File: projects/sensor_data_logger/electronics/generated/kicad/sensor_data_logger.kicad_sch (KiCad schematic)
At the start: 14 parts, among them J1 USB-C POWER, J2 UART DEBUG, Q1 Ideal Diode, U1 ESP32-S3-WROOM-1, U2 ICM-42688-P, U3 3V3 Buck

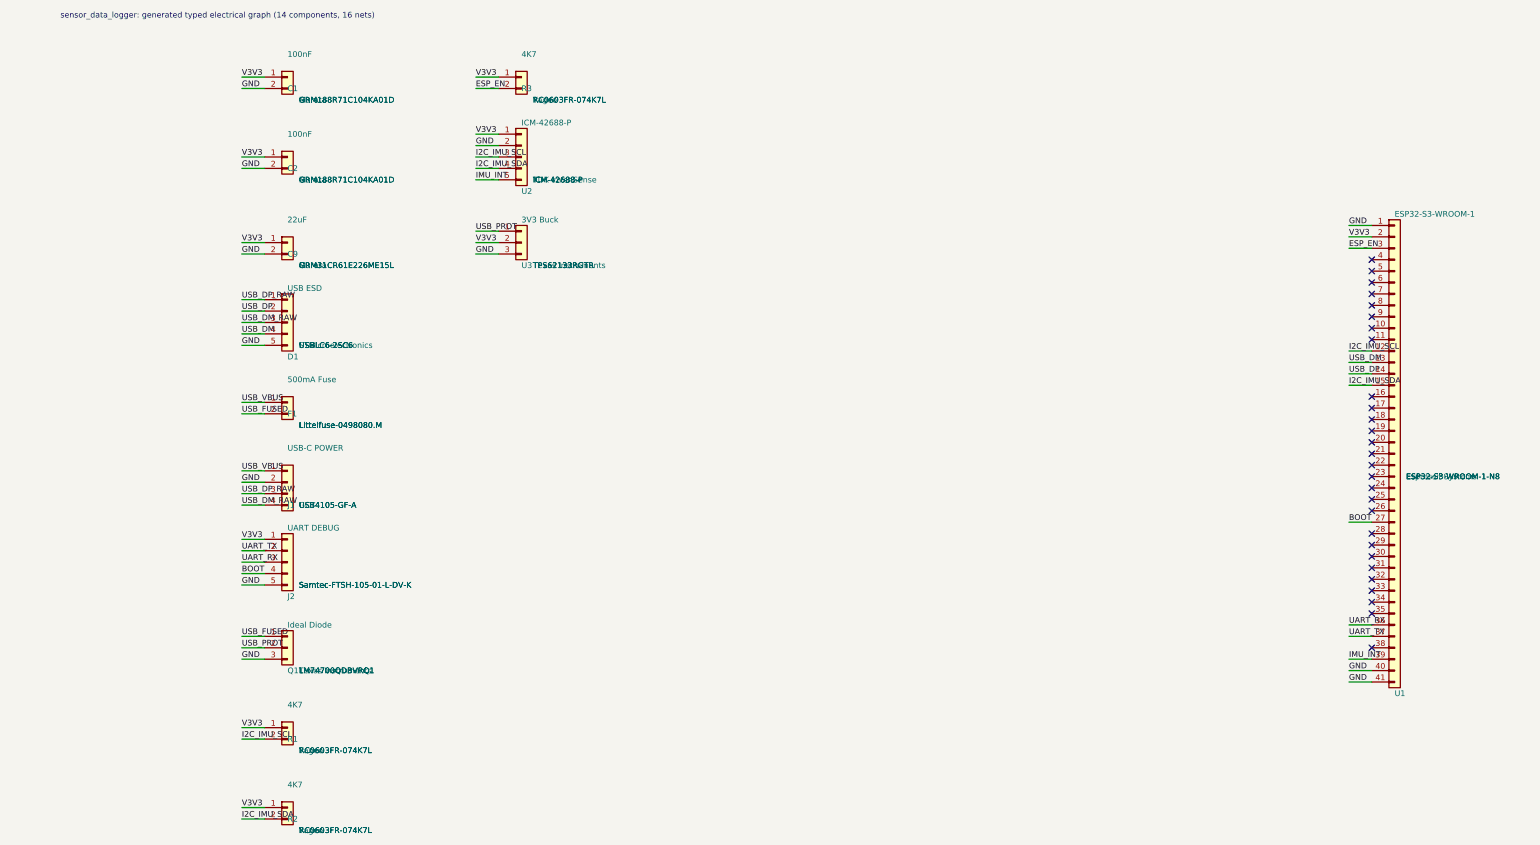
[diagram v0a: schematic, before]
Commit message: chore: regenerate sensor data logger artifacts
Regenerate electronics, mechanical, firmware, and validation outputs against the
UART debug connector, the fuse placement fix, and the 3D review preview. Adds the
3D-model-bearing KiCad board, the routed project files, and the new gate reports
(cross-domain consistency, mechanical connector cutouts/retention, mounting
integrity, DC operating point, power integrity, candidate critic, release).
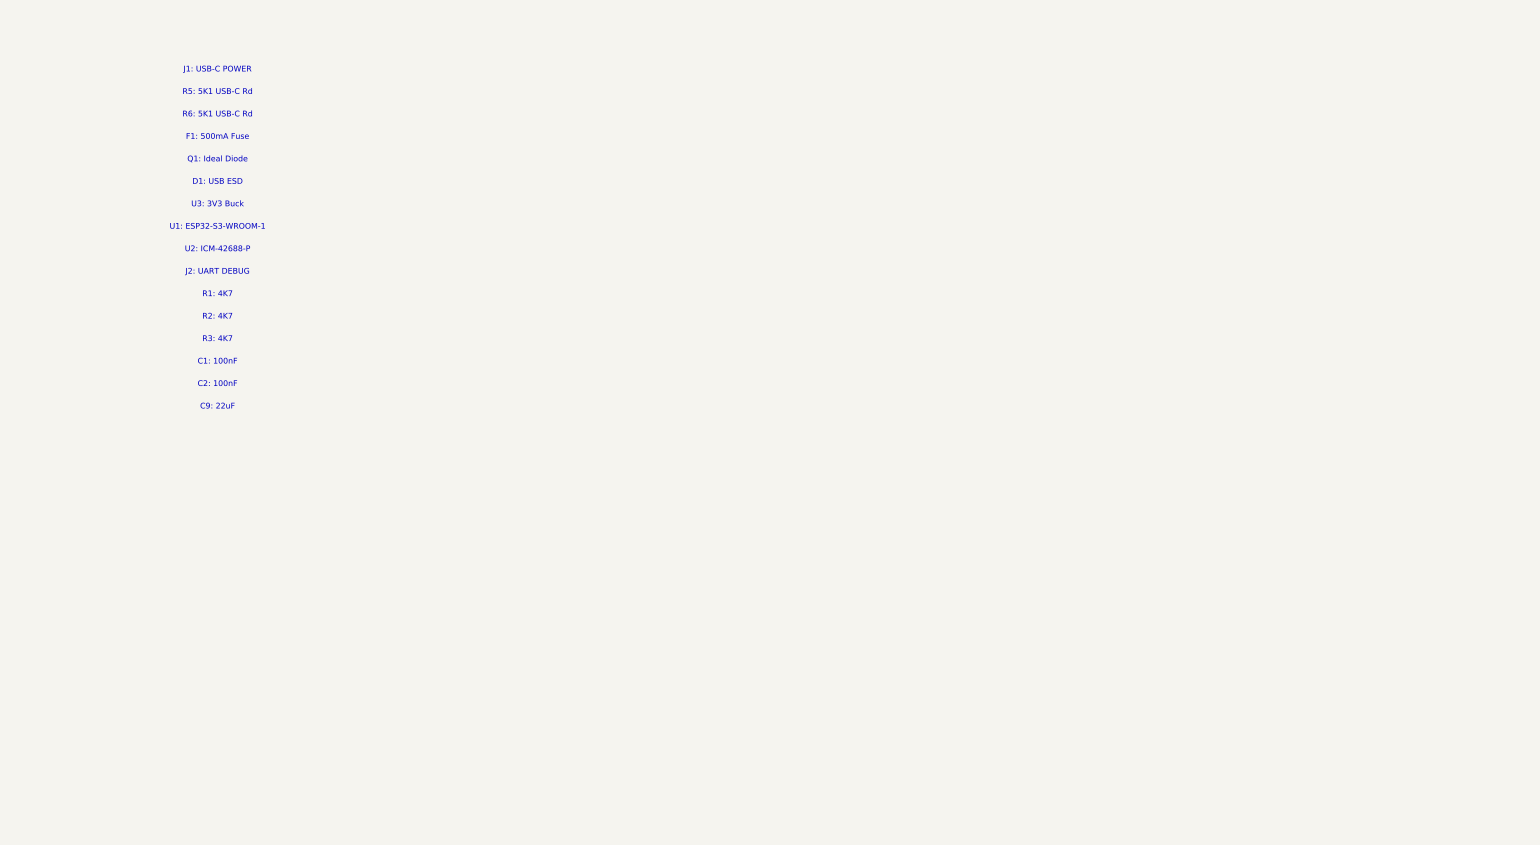
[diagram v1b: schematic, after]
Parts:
- removed C1, C2: 100nF, C0603, symbol Connector_Generic:Conn_01x02
- removed C9: 22uF, C1206, symbol Connector_Generic:Conn_01x02
- removed D1: USB ESD, SOT23-6, symbol Connector_Generic:Conn_01x05
- removed F1: 500mA Fuse, MIDI, symbol Connector_Generic:Conn_01x02
- removed J1: USB-C POWER, USB_C_16Pin, symbol Connector_Generic:Conn_01x04
- removed J2: UART DEBUG, Cortex_Debug_10Pin, symbol Connector_Generic:Conn_01x05
- removed Q1: Ideal Diode, SOT23-6, symbol Connector_Generic:Conn_01x03
- removed R1, R2, R3: 4K7, R0603, symbol Connector_Generic:Conn_01x02
- removed U1: ESP32-S3-WROOM-1, RF_Module:ESP32-S3-WROOM-1, symbol Connector_Generic:Conn_01x41
- removed U2: ICM-42688-P, LGA14, symbol Connector_Generic:Conn_01x05
- removed U3: 3V3 Buck, VQFN16, symbol Connector_Generic:Conn_01x03
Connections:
- no-connect marks 28 -> 0
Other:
- note added: "C1: 100nF"
- note added: "C2: 100nF"
- note added: "C9: 22uF"
- note added: "D1: USB ESD"
- note added: "F1: 500mA Fuse"
- note added: "J1: USB-C POWER"
- note added: "J2: UART DEBUG"
- note added: "Q1: Ideal Diode"
- note added: "R1: 4K7"
- note added: "R2: 4K7"
- note added: "R3: 4K7"
- note added: "R5: 5K1 USB-C Rd"
- note added: "R6: 5K1 USB-C Rd"
- note added: "U1: ESP32-S3-WROOM-1"
- note added: "U2: ICM-42688-P"
- note added: "U3: 3V3 Buck"
- note removed: "sensor_data_logger: generated typed electrical graph (14 components, 16 nets)"
- title: sensor_data_logger -> (none)
